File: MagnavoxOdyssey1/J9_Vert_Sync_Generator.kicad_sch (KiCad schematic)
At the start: 12 parts

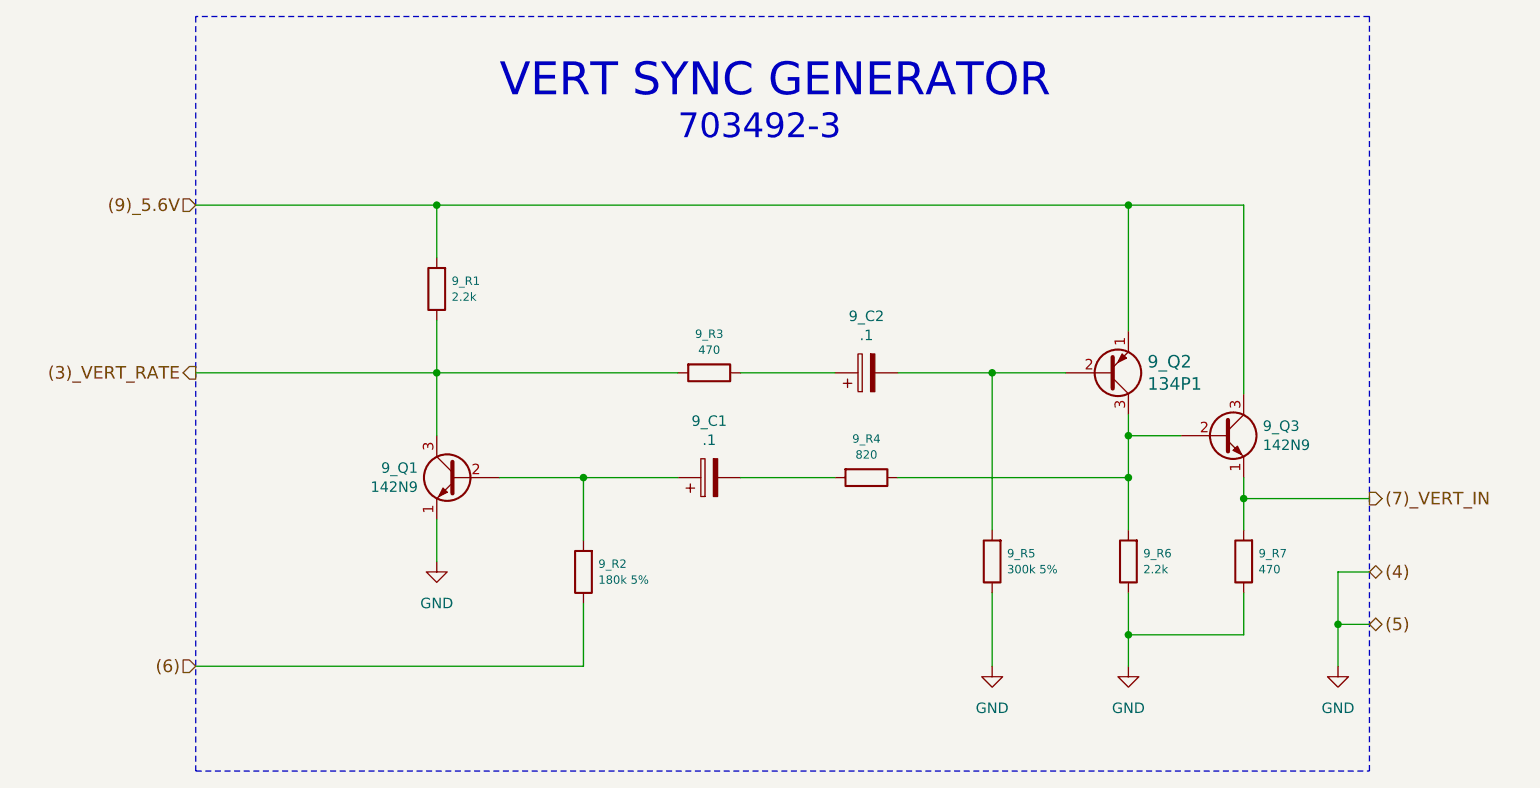
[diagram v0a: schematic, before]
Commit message: update to kicad 9
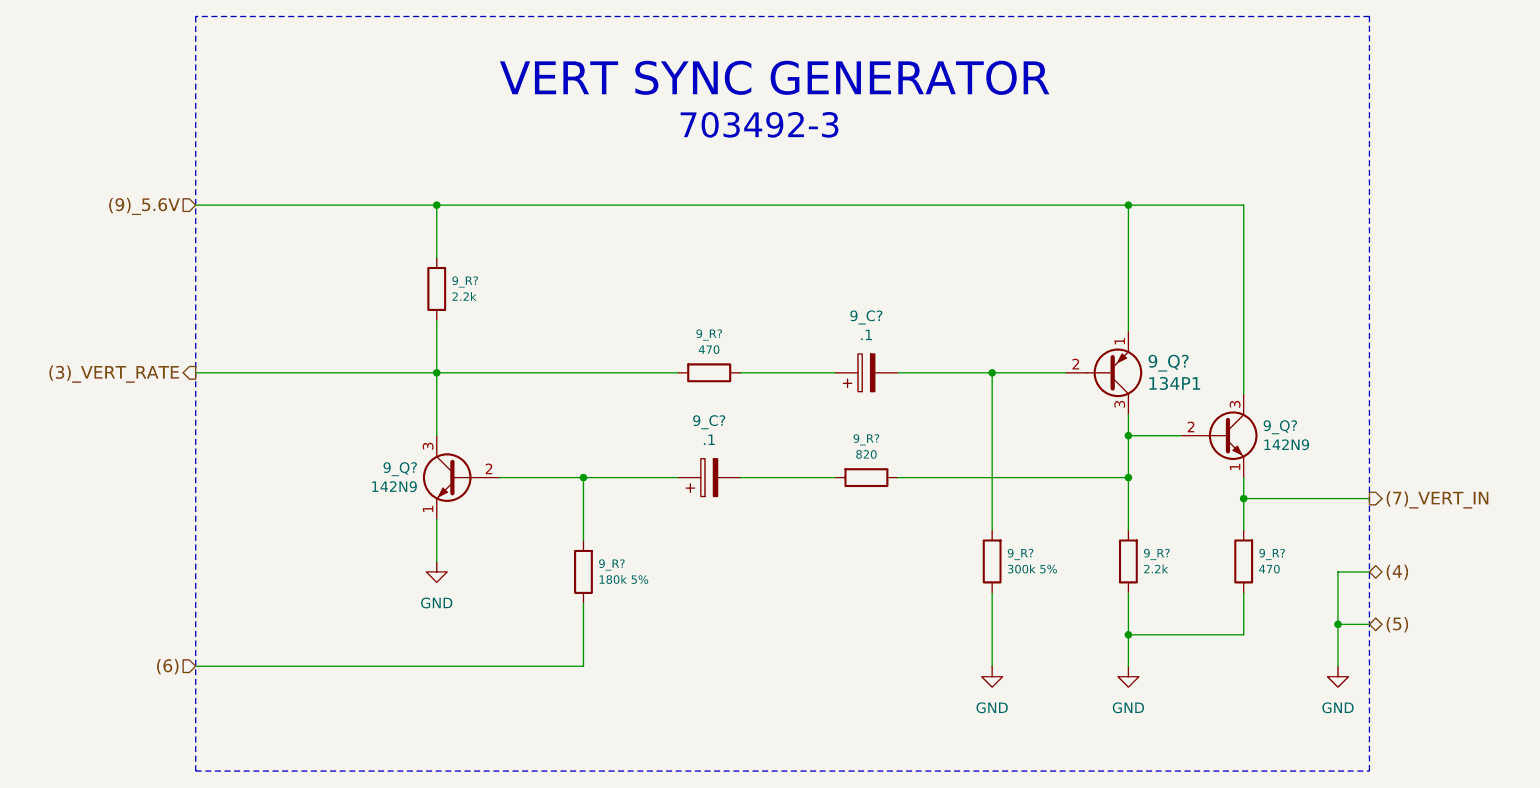
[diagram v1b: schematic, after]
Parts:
- 9_Q?: renamed from 9_Q1; symbol Device:Q_NPN_EBC -> Transistor_BJT:Q_NPN_EBC
- 9_Q?: renamed from 9_Q3; symbol Device:Q_NPN_EBC -> Transistor_BJT:Q_NPN_EBC
- 9_Q?: renamed from 9_Q2; symbol Device:Q_PNP_EBC -> Transistor_BJT:Q_PNP_EBC
- renumbered 9_C1 to 9_C?, 9_C2 to 9_C?, 9_R4 to 9_R?, 9_R2 to 9_R?, 9_R5 to 9_R?, 9_R3 to 9_R?, 9_R1 to 9_R?, 9_R6 to 9_R?, 9_R7 to 9_R?

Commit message: annotate
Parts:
- gave numbers to parts that had none: 12
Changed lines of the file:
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@@
 		(on_board yes)
 		(dnp no)
-		(property "Reference" "9_Q?"
+		(property "Reference" "9_Q3"
 			(at 103.124 108.0516 0)
 			(effects
@@
 			(project "MagnavoxOdyssey1"
 				(path "/adb6e295-eae5-402e-a614-02a705c3e27c/00000000-0000-0000-0000-00005890191b"
-					(reference "9_Q?")
+					(reference "9_Q3")
 					(unit 1)
 				)
@@
 		(on_board yes)
 		(dnp no)
-		(property "Reference" "9_Q?"
+		(property "Reference" "9_Q2"
 			(at 205.5114 102.9716 0)
 			(effects
@@
 			(project "MagnavoxOdyssey1"
 				(path "/adb6e295-eae5-402e-a614-02a705c3e27c/00000000-0000-0000-0000-00005890191b"
-					(reference "9_Q?")
+					(reference "9_Q2")
 					(unit 1)
 				)
@@
 		(on_board yes)
 		(dnp no)
-		(property "Reference" "9_Q?"
+		(property "Reference" "9_Q1"
 			(at 191.5414 95.1738 0)
 			(effects
@@
 			(project "MagnavoxOdyssey1"
 				(path "/adb6e295-eae5-402e-a614-02a705c3e27c/00000000-0000-0000-0000-00005890191b"
-					(reference "9_Q?")
+					(reference "9_Q1")
 					(unit 1)
 				)
@@
 		(on_board yes)
 		(dnp no)
-		(property "Reference" "9_C?"
+		(property "Reference" "9_C2"
 			(at 138.43 102.362 90)
 			(effects
@@
 			(project "MagnavoxOdyssey1"
 				(path "/adb6e295-eae5-402e-a614-02a705c3e27c/00000000-0000-0000-0000-00005890191b"
-					(reference "9_C?")
+					(reference "9_C2")
 					(unit 1)
 				)
@@
 		(on_board yes)
 		(dnp no)
-		(property "Reference" "9_R?"
+		(property "Reference" "9_R3"
 			(at 157.48 104.521 90)
 			(effects
@@
 			(project "MagnavoxOdyssey1"
 				(path "/adb6e295-eae5-402e-a614-02a705c3e27c/00000000-0000-0000-0000-00005890191b"
-					(reference "9_R?")
+					(reference "9_R3")
 					(unit 1)
 				)
@@
 		(on_board yes)
 		(dnp no)
-		(property "Reference" "9_R?"
+		(property "Reference" "9_R7"
 			(at 124.9934 119.6848 0)
 			(effects
@@
 			(project "MagnavoxOdyssey1"
 				(path "/adb6e295-eae5-402e-a614-02a705c3e27c/00000000-0000-0000-0000-00005890191b"
-					(reference "9_R?")
+					(reference "9_R7")
 					(unit 1)
 				)
@@
 		(on_board yes)
 		(dnp no)
-		(property "Reference" "9_R?"
+		(property "Reference" "9_R4"
 			(at 174.5234 118.4148 0)
 			(effects
@@
 			(project "MagnavoxOdyssey1"
 				(path "/adb6e295-eae5-402e-a614-02a705c3e27c/00000000-0000-0000-0000-00005890191b"
-					(reference "9_R?")
+					(reference "9_R4")
 					(unit 1)
 				)
@@
 		(on_board yes)
 		(dnp no)
-		(property "Reference" "9_R?"
+		(property "Reference" "9_R2"
 			(at 138.43 91.821 90)
 			(effects
@@
 			(project "MagnavoxOdyssey1"
 				(path "/adb6e295-eae5-402e-a614-02a705c3e27c/00000000-0000-0000-0000-00005890191b"
-					(reference "9_R?")
+					(reference "9_R2")
 					(unit 1)
 				)
@@
 		(on_board yes)
 		(dnp no)
-		(property "Reference" "9_C?"
+		(property "Reference" "9_C1"
 			(at 157.48 89.662 90)
 			(effects
@@
 			(project "MagnavoxOdyssey1"
 				(path "/adb6e295-eae5-402e-a614-02a705c3e27c/00000000-0000-0000-0000-00005890191b"
-					(reference "9_C?")
+					(reference "9_C1")
 					(unit 1)
 				)
@@
 		(on_board yes)
 		(dnp no)
-		(property "Reference" "9_R?"
+		(property "Reference" "9_R1"
 			(at 107.2134 85.3948 0)
 			(effects
@@
 			(project "MagnavoxOdyssey1"
 				(path "/adb6e295-eae5-402e-a614-02a705c3e27c/00000000-0000-0000-0000-00005890191b"
-					(reference "9_R?")
+					(reference "9_R1")
 					(unit 1)
 				)
@@
 		(on_board yes)
 		(dnp no)
-		(property "Reference" "9_R?"
+		(property "Reference" "9_R5"
 			(at 191.0334 118.4148 0)
 			(effects
@@
 			(project "MagnavoxOdyssey1"
 				(path "/adb6e295-eae5-402e-a614-02a705c3e27c/00000000-0000-0000-0000-00005890191b"
-					(reference "9_R?")
+					(reference "9_R5")
 					(unit 1)
 				)
@@
 		(on_board yes)
 		(dnp no)
-		(property "Reference" "9_R?"
+		(property "Reference" "9_R6"
 			(at 205.0034 118.4148 0)
 			(effects
@@
 			(project "MagnavoxOdyssey1"
 				(path "/adb6e295-eae5-402e-a614-02a705c3e27c/00000000-0000-0000-0000-00005890191b"
-					(reference "9_R?")
-					(unit 1)
-				)
+					(reference "9_R6")
+					(unit 1)
+				)

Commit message: accurate resistors
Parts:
- 9_R4: value 300k 5% -> 300k
- 9_R7: value 180k 5% -> 180k
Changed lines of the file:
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@@
 			)
 		)
-		(property "Value" "180k 5%"
+		(property "Value" "180k"
 			(at 124.9934 121.6152 0)
 			(effects
@@
 			)
 		)
-		(property "Value" "300k 5%"
+		(property "Value" "300k"
 			(at 174.5234 120.3452 0)
 			(effects
